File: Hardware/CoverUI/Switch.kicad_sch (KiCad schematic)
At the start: 18 parts, among them SW1 SW_MEC_5G, SW10 SW_MEC_5G, SW11 SW_MEC_5G, SW12 SW_MEC_5G, SW13 SW_MEC_5G, SW14 SW_MEC_5G, SW2 SW_MEC_5G, SW3 SW_MEC_5G, SW4 SW_MEC_5G, SW5 SW_MEC_5G, SW6 SW_MEC_5G, SW7 SW_MEC_5G, SW8 SW_MEC_5G, SW9 SW_MEC_5G

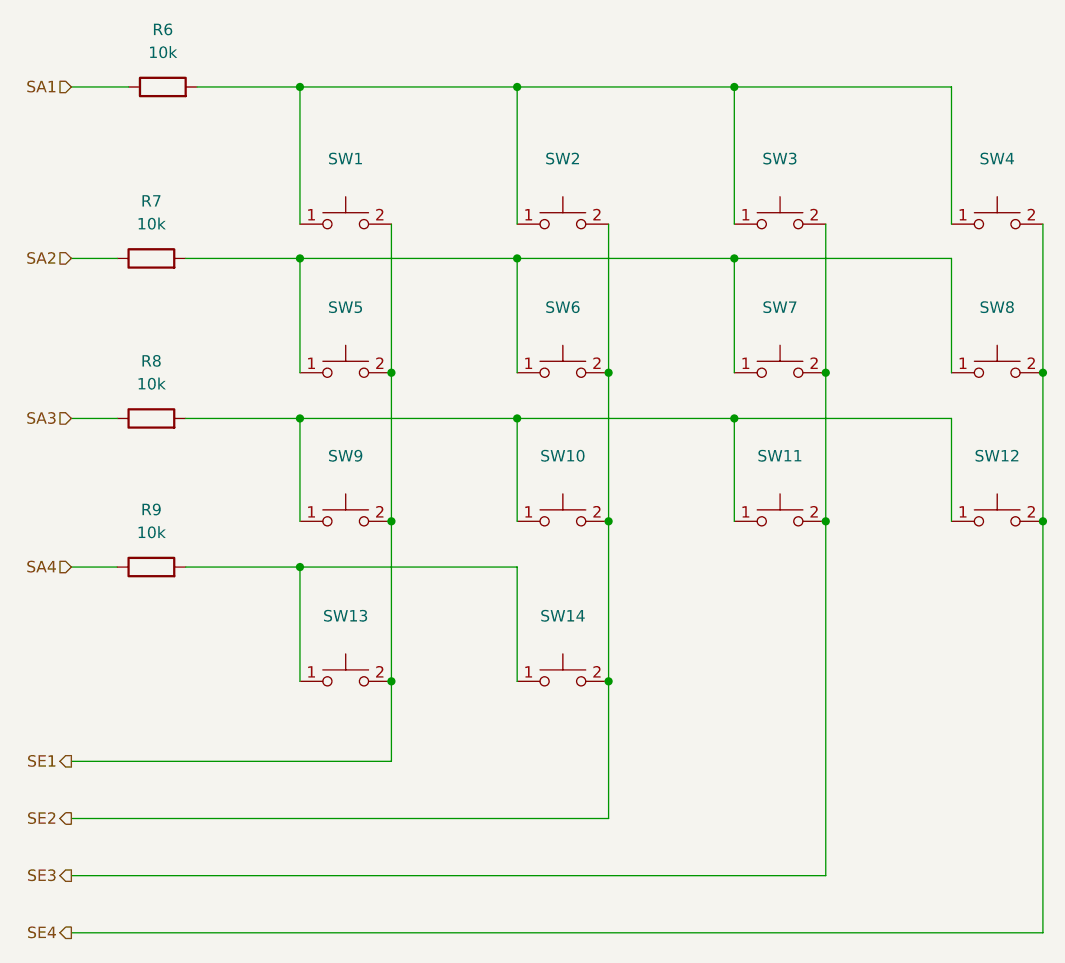
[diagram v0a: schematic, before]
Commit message: fix(ui): update switch footprints, make central hole smaller
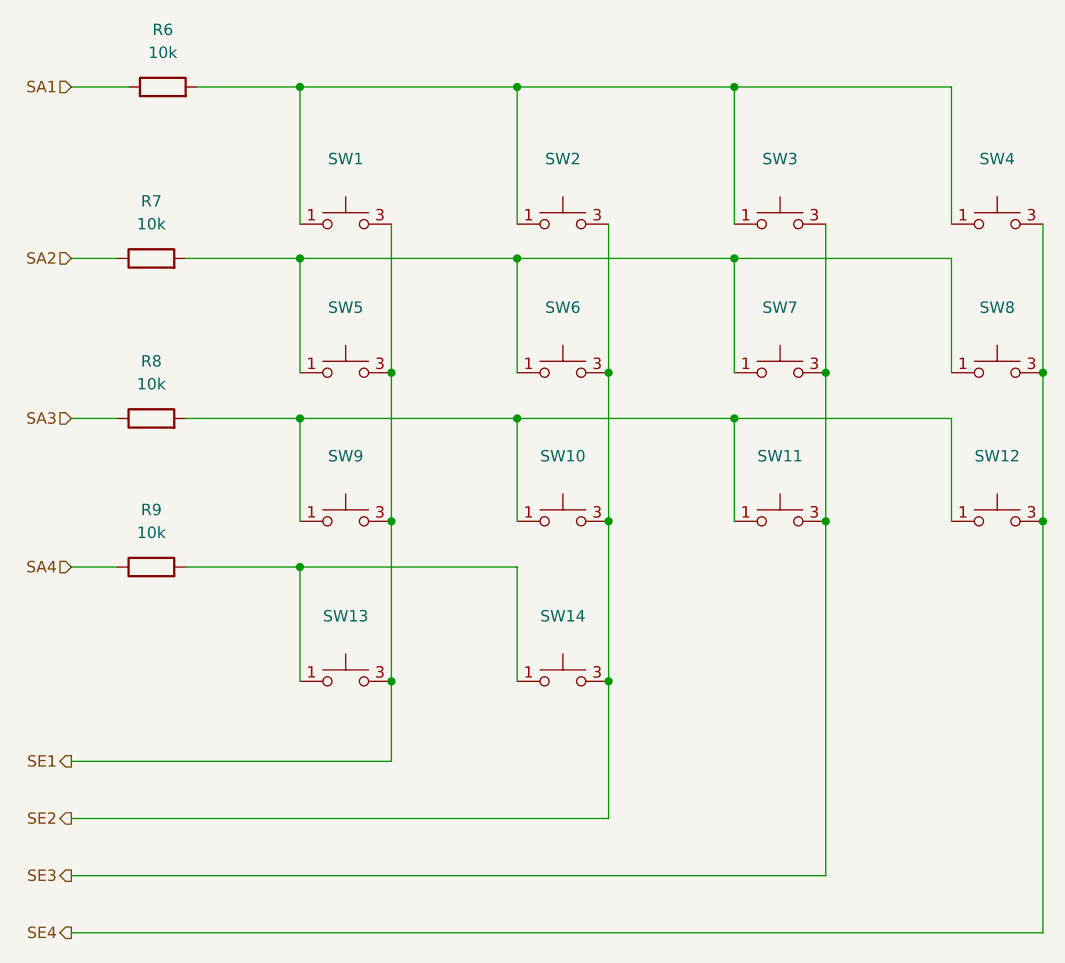
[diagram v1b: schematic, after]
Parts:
- SW1, SW10, SW11, SW12, SW13, SW14, SW2, SW3, SW4, SW5, SW6, SW7, SW8, SW9: footprint Button_Switch_SMD:SW_SPST_TL3305A -> lcsc:KEY-SMD_4P-L6.0-W6.0-P3.90-LS9.0
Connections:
- net SE1: now also SW1.3 (B), SW13.3 (B), SW5.3 (B), SW9.3 (B); no longer SW1.2 (B), SW13.2 (B), SW5.2 (B), SW9.2 (B)
- net SE2: now also SW10.3 (B), SW14.3 (B), SW2.3 (B), SW6.3 (B); no longer SW10.2 (B), SW14.2 (B), SW2.2 (B), SW6.2 (B)
- net SE3: now also SW11.3 (B), SW3.3 (B), SW7.3 (B); no longer SW11.2 (B), SW3.2 (B), SW7.2 (B)
- net SE4: now also SW12.3 (B), SW4.3 (B), SW8.3 (B); no longer SW12.2 (B), SW4.2 (B), SW8.2 (B)

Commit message: fix(ui): update switches to 4.5mm
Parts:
- SW1, SW10, SW11, SW12, SW13, SW14, SW2, SW3, SW4, SW5, SW6, SW7, SW8, SW9: footprint lcsc:KEY-SMD_4P-L6.0-W6.0-P3.90-LS9.0 -> lcsc:SW-SMD_4P-L4.5-W4.5-P3.00-LS7.0; LCSC Part C2834928 -> C840835
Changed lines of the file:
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@@
       (effects (font (size 1.27 1.27)) hide)
     )
-    (property "Footprint" "lcsc:KEY-SMD_4P-L6.0-W6.0-P3.90-LS9.0" (id 2) (at 144.78 53.34 0)
+    (property "Footprint" "lcsc:SW-SMD_4P-L4.5-W4.5-P3.00-LS7.0" (id 2) (at 144.78 53.34 0)
       (effects (font (size 1.27 1.27)) hide)
     )
@@
       (effects (font (size 1.27 1.27)) hide)
     )
-    (property "LCSC Part" "C2834928" (id 4) (at 144.78 58.42 0)
+    (property "LCSC Part" "C840835" (id 4) (at 144.78 58.42 0)
       (effects (font (size 1.27 1.27)) hide)
     )
@@
       (effects (font (size 1.27 1.27)) hide)
     )
-    (property "Footprint" "lcsc:KEY-SMD_4P-L6.0-W6.0-P3.90-LS9.0" (id 2) (at 120.65 36.83 0)
+    (property "Footprint" "lcsc:SW-SMD_4P-L4.5-W4.5-P3.00-LS7.0" (id 2) (at 120.65 36.83 0)
       (effects (font (size 1.27 1.27)) hide)
     )
@@
       (effects (font (size 1.27 1.27)) hide)
     )
-    (property "LCSC Part" "C2834928" (id 4) (at 120.65 41.91 0)
+    (property "LCSC Part" "C840835" (id 4) (at 120.65 41.91 0)
       (effects (font (size 1.27 1.27)) hide)
     )
@@
       (effects (font (size 1.27 1.27)) hide)
     )
-    (property "Footprint" "lcsc:KEY-SMD_4P-L6.0-W6.0-P3.90-LS9.0" (id 2) (at 168.91 36.83 0)
+    (property "Footprint" "lcsc:SW-SMD_4P-L4.5-W4.5-P3.00-LS7.0" (id 2) (at 168.91 36.83 0)
       (effects (font (size 1.27 1.27)) hide)
     )
@@
       (effects (font (size 1.27 1.27)) hide)
     )
-    (property "LCSC Part" "C2834928" (id 4) (at 168.91 41.91 0)
+    (property "LCSC Part" "C840835" (id 4) (at 168.91 41.91 0)
       (effects (font (size 1.27 1.27)) hide)
     )
@@
       (effects (font (size 1.27 1.27)) hide)
     )
-    (property "Footprint" "lcsc:KEY-SMD_4P-L6.0-W6.0-P3.90-LS9.0" (id 2) (at 193.04 69.85 0)
+    (property "Footprint" "lcsc:SW-SMD_4P-L4.5-W4.5-P3.00-LS7.0" (id 2) (at 193.04 69.85 0)
       (effects (font (size 1.27 1.27)) hide)
     )
@@
       (effects (font (size 1.27 1.27)) hide)
     )
-    (property "LCSC Part" "C2834928" (id 4) (at 193.04 74.93 0)
+    (property "LCSC Part" "C840835" (id 4) (at 193.04 74.93 0)
       (effects (font (size 1.27 1.27)) hide)
     )
@@
       (effects (font (size 1.27 1.27)) hide)
     )
-    (property "Footprint" "lcsc:KEY-SMD_4P-L6.0-W6.0-P3.90-LS9.0" (id 2) (at 144.78 36.83 0)
+    (property "Footprint" "lcsc:SW-SMD_4P-L4.5-W4.5-P3.00-LS7.0" (id 2) (at 144.78 36.83 0)
       (effects (font (size 1.27 1.27)) hide)
     )
@@
       (effects (font (size 1.27 1.27)) hide)
     )
-    (property "LCSC Part" "C2834928" (id 4) (at 144.78 41.91 0)
+    (property "LCSC Part" "C840835" (id 4) (at 144.78 41.91 0)
       (effects (font (size 1.27 1.27)) hide)
     )
@@
       (effects (font (size 1.27 1.27)) hide)
     )
-    (property "Footprint" "lcsc:KEY-SMD_4P-L6.0-W6.0-P3.90-LS9.0" (id 2) (at 120.65 53.34 0)
+    (property "Footprint" "lcsc:SW-SMD_4P-L4.5-W4.5-P3.00-LS7.0" (id 2) (at 120.65 53.34 0)
       (effects (font (size 1.27 1.27)) hide)
     )
@@
       (effects (font (size 1.27 1.27)) hide)
     )
-    (property "LCSC Part" "C2834928" (id 4) (at 120.65 58.42 0)
+    (property "LCSC Part" "C840835" (id 4) (at 120.65 58.42 0)
       (effects (font (size 1.27 1.27)) hide)
     )
@@
       (effects (font (size 1.27 1.27)) hide)
     )
-    (property "Footprint" "lcsc:KEY-SMD_4P-L6.0-W6.0-P3.90-LS9.0" (id 2) (at 120.65 69.85 0)
+    (property "Footprint" "lcsc:SW-SMD_4P-L4.5-W4.5-P3.00-LS7.0" (id 2) (at 120.65 69.85 0)
       (effects (font (size 1.27 1.27)) hide)
     )
@@
       (effects (font (size 1.27 1.27)) hide)
     )
-    (property "LCSC Part" "C2834928" (id 4) (at 120.65 74.93 0)
+    (property "LCSC Part" "C840835" (id 4) (at 120.65 74.93 0)
       (effects (font (size 1.27 1.27)) hide)
     )
@@
       (effects (font (size 1.27 1.27)) hide)
     )
-    (property "Footprint" "lcsc:KEY-SMD_4P-L6.0-W6.0-P3.90-LS9.0" (id 2) (at 120.65 87.63 0)
+    (property "Footprint" "lcsc:SW-SMD_4P-L4.5-W4.5-P3.00-LS7.0" (id 2) (at 120.65 87.63 0)
       (effects (font (size 1.27 1.27)) hide)
     )
@@
       (effects (font (size 1.27 1.27)) hide)
     )
-    (property "LCSC Part" "C2834928" (id 4) (at 120.65 92.71 0)
+    (property "LCSC Part" "C840835" (id 4) (at 120.65 92.71 0)
       (effects (font (size 1.27 1.27)) hide)
     )
@@
       (effects (font (size 1.27 1.27)) hide)
     )
-    (property "Footprint" "lcsc:KEY-SMD_4P-L6.0-W6.0-P3.90-LS9.0" (id 2) (at 168.91 53.34 0)
+    (property "Footprint" "lcsc:SW-SMD_4P-L4.5-W4.5-P3.00-LS7.0" (id 2) (at 168.91 53.34 0)
       (effects (font (size 1.27 1.27)) hide)
     )
@@
       (effects (font (size 1.27 1.27)) hide)
     )
-    (property "LCSC Part" "C2834928" (id 4) (at 168.91 58.42 0)
+    (property "LCSC Part" "C840835" (id 4) (at 168.91 58.42 0)
       (effects (font (size 1.27 1.27)) hide)
     )
@@
       (effects (font (size 1.27 1.27)) hide)
     )
-    (property "Footprint" "lcsc:KEY-SMD_4P-L6.0-W6.0-P3.90-LS9.0" (id 2) (at 144.78 87.63 0)
+    (property "Footprint" "lcsc:SW-SMD_4P-L4.5-W4.5-P3.00-LS7.0" (id 2) (at 144.78 87.63 0)
       (effects (font (size 1.27 1.27)) hide)
     )
@@
       (effects (font (size 1.27 1.27)) hide)
     )
-    (property "LCSC Part" "C2834928" (id 4) (at 144.78 92.71 0)
+    (property "LCSC Part" "C840835" (id 4) (at 144.78 92.71 0)
       (effects (font (size 1.27 1.27)) hide)
     )
@@
       (effects (font (size 1.27 1.27)) hide)
     )
-    (property "Footprint" "lcsc:KEY-SMD_4P-L6.0-W6.0-P3.90-LS9.0" (id 2) (at 168.91 69.85 0)
+    (property "Footprint" "lcsc:SW-SMD_4P-L4.5-W4.5-P3.00-LS7.0" (id 2) (at 168.91 69.85 0)
       (effects (font (size 1.27 1.27)) hide)
     )
@@
       (effects (font (size 1.27 1.27)) hide)
     )
-    (property "LCSC Part" "C2834928" (id 4) (at 168.91 74.93 0)
+    (property "LCSC Part" "C840835" (id 4) (at 168.91 74.93 0)
       (effects (font (size 1.27 1.27)) hide)
     )
@@
       (effects (font (size 1.27 1.27)) hide)
     )
-    (property "Footprint" "lcsc:KEY-SMD_4P-L6.0-W6.0-P3.90-LS9.0" (id 2) (at 193.04 36.83 0)
+    (property "Footprint" "lcsc:SW-SMD_4P-L4.5-W4.5-P3.00-LS7.0" (id 2) (at 193.04 36.83 0)
       (effects (font (size 1.27 1.27)) hide)
     )
@@
       (effects (font (size 1.27 1.27)) hide)
     )
-    (property "LCSC Part" "C2834928" (id 4) (at 193.04 41.91 0)
+    (property "LCSC Part" "C840835" (id 4) (at 193.04 41.91 0)
       (effects (font (size 1.27 1.27)) hide)
     )
@@
       (effects (font (size 1.27 1.27)) hide)
     )
-    (property "Footprint" "lcsc:KEY-SMD_4P-L6.0-W6.0-P3.90-LS9.0" (id 2) (at 193.04 53.34 0)
+    (property "Footprint" "lcsc:SW-SMD_4P-L4.5-W4.5-P3.00-LS7.0" (id 2) (at 193.04 53.34 0)
       (effects (font (size 1.27 1.27)) hide)
     )
@@
       (effects (font (size 1.27 1.27)) hide)
     )
-    (property "LCSC Part" "C2834928" (id 4) (at 193.04 58.42 0)
+    (property "LCSC Part" "C840835" (id 4) (at 193.04 58.42 0)
       (effects (font (size 1.27 1.27)) hide)
     )
@@
       (effects (font (size 1.27 1.27)) hide)
     )
-    (property "Footprint" "lcsc:KEY-SMD_4P-L6.0-W6.0-P3.90-LS9.0" (id 2) (at 144.78 69.85 0)
+    (property "Footprint" "lcsc:SW-SMD_4P-L4.5-W4.5-P3.00-LS7.0" (id 2) (at 144.78 69.85 0)
       (effects (font (size 1.27 1.27)) hide)
     )
@@
       (effects (font (size 1.27 1.27)) hide)
     )
-    (property "LCSC Part" "C2834928" (id 4) (at 144.78 74.93 0)
-      (effects (font (size 1.27 1.27)) hide)
-    )
+    (property "LCSC Part" "C840835" (id 4) (at 144.78 74.93 0)
+      (effects (font (size 1.27 1.27)) hide)
+    )
